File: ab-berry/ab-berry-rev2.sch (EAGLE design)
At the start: 66 parts, among them IC1 STM32F302RCT6, U1 LM1117MPX-3.3/NOPB or AP2114H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

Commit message: wip
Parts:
- removed STM32F072CBT6: STM32F072-LQFP48, stm32f0:STM32F072-LQFP48
- added R23, R24: 22, microbuilder:RESISTOR0603
- added X1: (no value), keves:TE-292304-1
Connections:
- new net N$18: R23.2, X1_CONN.2
- new net N$19: R24.2, X1_CONN.3
- new net SPI1_SCK: IC1.PB3, LCD2.CLK
- new net USB_DM: IC1.PA11, R23.1
- new net USB_DP: IC1.PA12, R24.1
- net 5.0V: now also X1_CONN.1
- net BTN_USR: now also IC1.PC13; no longer STM32F072CBT6.PC13/WKUP2/RTC_TAMP1/RTC_TS/RTC_OUT
- net CAN_RX: now also IC1.PB8; no longer STM32F072CBT6.PA11/USB_DM/CAN_RX
- net CAN_TX: now also IC1.PB9; no longer STM32F072CBT6.PA12/USB_DP/CAN_TX
- net DBG_RX: no longer STM32F072CBT6.PA10/USART1_RX/TIM1_CH3
- net DBG_TX: no longer STM32F072CBT6.PA9/USART1_TX/TIM1_CH2
- net GND: now also X1_CONN.4
- net LCD_CS1: now also IC1.PC11; no longer STM32F072CBT6.PB2
- net LCD_CS2: now also IC1.PC12; no longer STM32F072CBT6.PB1/ADC_IN9/TIM3_CH4
- net LCD_DC: now also IC1.PB7; no longer STM32F072CBT6.PA4/ADC_IN4/DAC_OUT1
- net LCD_RST: now also IC1.PB6; no longer STM32F072CBT6.PA3/ADC_IN3/COMP2_INP/USART2_RX
- net N$6: no longer STM32F072CBT6.PB0/ADC_IN8/TIM3_CH3
- net N$8: now also IC1.PF0_OSCIN; no longer STM32F072CBT6.PF0/OSC_IN
- net N$9: now also IC1.PF1_OSCOUT; no longer STM32F072CBT6.PF1/OSC_OUT
- net ROT1_A: no longer STM32F072CBT6.PB14/SPI2_MISO/I2C2_SDA
- net ROT1_B: no longer STM32F072CBT6.PB15/WKUP7/RTC_REFIN/SPI2_MOSI
- net ROT1_SW: no longer STM32F072CBT6.PB12
- net ROT2_A: no longer STM32F072CBT6.PB4/SPI1_MISO/TIM3_CH1
- net ROT2_B: no longer STM32F072CBT6.PB5/WKUP6/SPI1_MOSI/TIM3_CH2
- net ROT2_SW: no longer STM32F072CBT6.PB3/SPI1_SCK/TIM2_CH2
- net ROT3_A: no longer STM32F072CBT6.PB7/USART1_RX/I2C1_SDA
- net ROT3_B: no longer STM32F072CBT6.PB8/I2C1_SCL/TIM16_CH1/CAN_RX
- net ROT3_SW: no longer STM32F072CBT6.PB6USART1_TX/I2C1_SCL
- net ROT4_A: no longer STM32F072CBT6.PB13/SPI2_SCK/I2C2_SCL
- net ROT4_B: no longer STM32F072CBT6.PB11/I2C2_SDA/TIM2_C4/USART3_RX
- net ROT4_SW: no longer STM32F072CBT6.PB10/I2C2_SCL/TIM2_CH3/USART3_TX
- net SPI1_CLK: no longer LCD2.CLK, STM32F072CBT6.PA5/ADC_IN5/DAC_OUT2/SPI1_SCK
- net SPI1_MOSI: now also IC1.PB5; no longer STM32F072CBT6.PA7/ADC_IN7/SPI1_MOSI/TIM3_CH2
- net SWCLK: no longer STM32F072CBT6.PA14/USART2_TX/SWCLK
- net SWDIO: no longer STM32F072CBT6.PA13/SWDIO
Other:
- note added: "TODO: - Verify USB resistors / DP/DM - Verify Boot0 and are there any other mandatory connections"
- moved on the sheet: C12, C13, U$36

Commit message: wip
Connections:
- net DBG_RX: now also IC1.PB11
- net DBG_TX: now also IC1.PB10
- net N$6: now also IC1.PB12
- net ROT1_A: now also IC1.PA2
- net ROT1_B: now also IC1.PA1
- net ROT1_SW: now also IC1.PA0
- net ROT2_A: now also IC1.PC7
- net ROT2_B: now also IC1.PC9
- net ROT2_SW: now also IC1.PC8
- net ROT3_A: now also IC1.PA9
- net ROT3_B: now also IC1.PA10
- net ROT3_SW: now also IC1.PA8
- net ROT4_A: now also IC1.PC2
- net ROT4_B: now also IC1.PC1
- net ROT4_SW: now also IC1.PC0
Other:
- note added: "TODO: - Verify USB resistors / DP/DM - Verify Boot0 and are there any other mandatory connections - USB shield + ESD"
- note removed: "TODO: - Verify USB resistors / DP/DM - Verify Boot0 and are there any other mandatory connections"
- moved on the sheet: C1, C12, C13, C2, C22, C3, C4, C5, C6, IC1, LED2, R1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

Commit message: wip
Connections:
- removed net SPI1_CLK: LCD1.CLK
- net SPI1_SCK: now also LCD1.CLK
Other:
- note added: "TODO: - Verify USB resistors / DP/DM - Verify Boot0 and are there any other mandatory connections - USB shield + ESD - Serial Flash"
- note removed: "TODO: - Verify USB resistors / DP/DM - Verify Boot0 and are there any other mandatory connections - USB shield + ESD"
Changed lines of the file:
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@@
 - Verify USB resistors / DP/DM
 - Verify Boot0 and are there any other mandatory connections
-- USB shield + ESD</text>
+- USB shield + ESD
+- Serial Flash</text>
 </plain>
 <instances>
@@
 </segment>
 </net>
-<net name="SPI1_CLK" class="0">
-<segment>
-<pinref part="LCD1" gate="G$1" pin="CLK"/>
-<wire x1="111.76" y1="-20.32" x2="99.06" y2="-20.32" width="0.1524" layer="91"/>
-<label x="91.44" y="-20.32" size="1.778" layer="95"/>
-</segment>
-</net>
 <net name="LCD_CS2" class="0">
 <segment>
@@
 <label x="91.44" y="-55.88" size="1.778" layer="95"/>
 </segment>
-</net>
+<segment>
+<pinref part="LCD1" gate="G$1" pin="CLK"/>
+<wire x1="111.76" y1="-20.32" x2="99.06" y2="-20.32" width="0.1524" layer="91"/>
+<label x="91.44" y="-20.32" size="1.778" layer="95"/>
+</segment>
+</net>

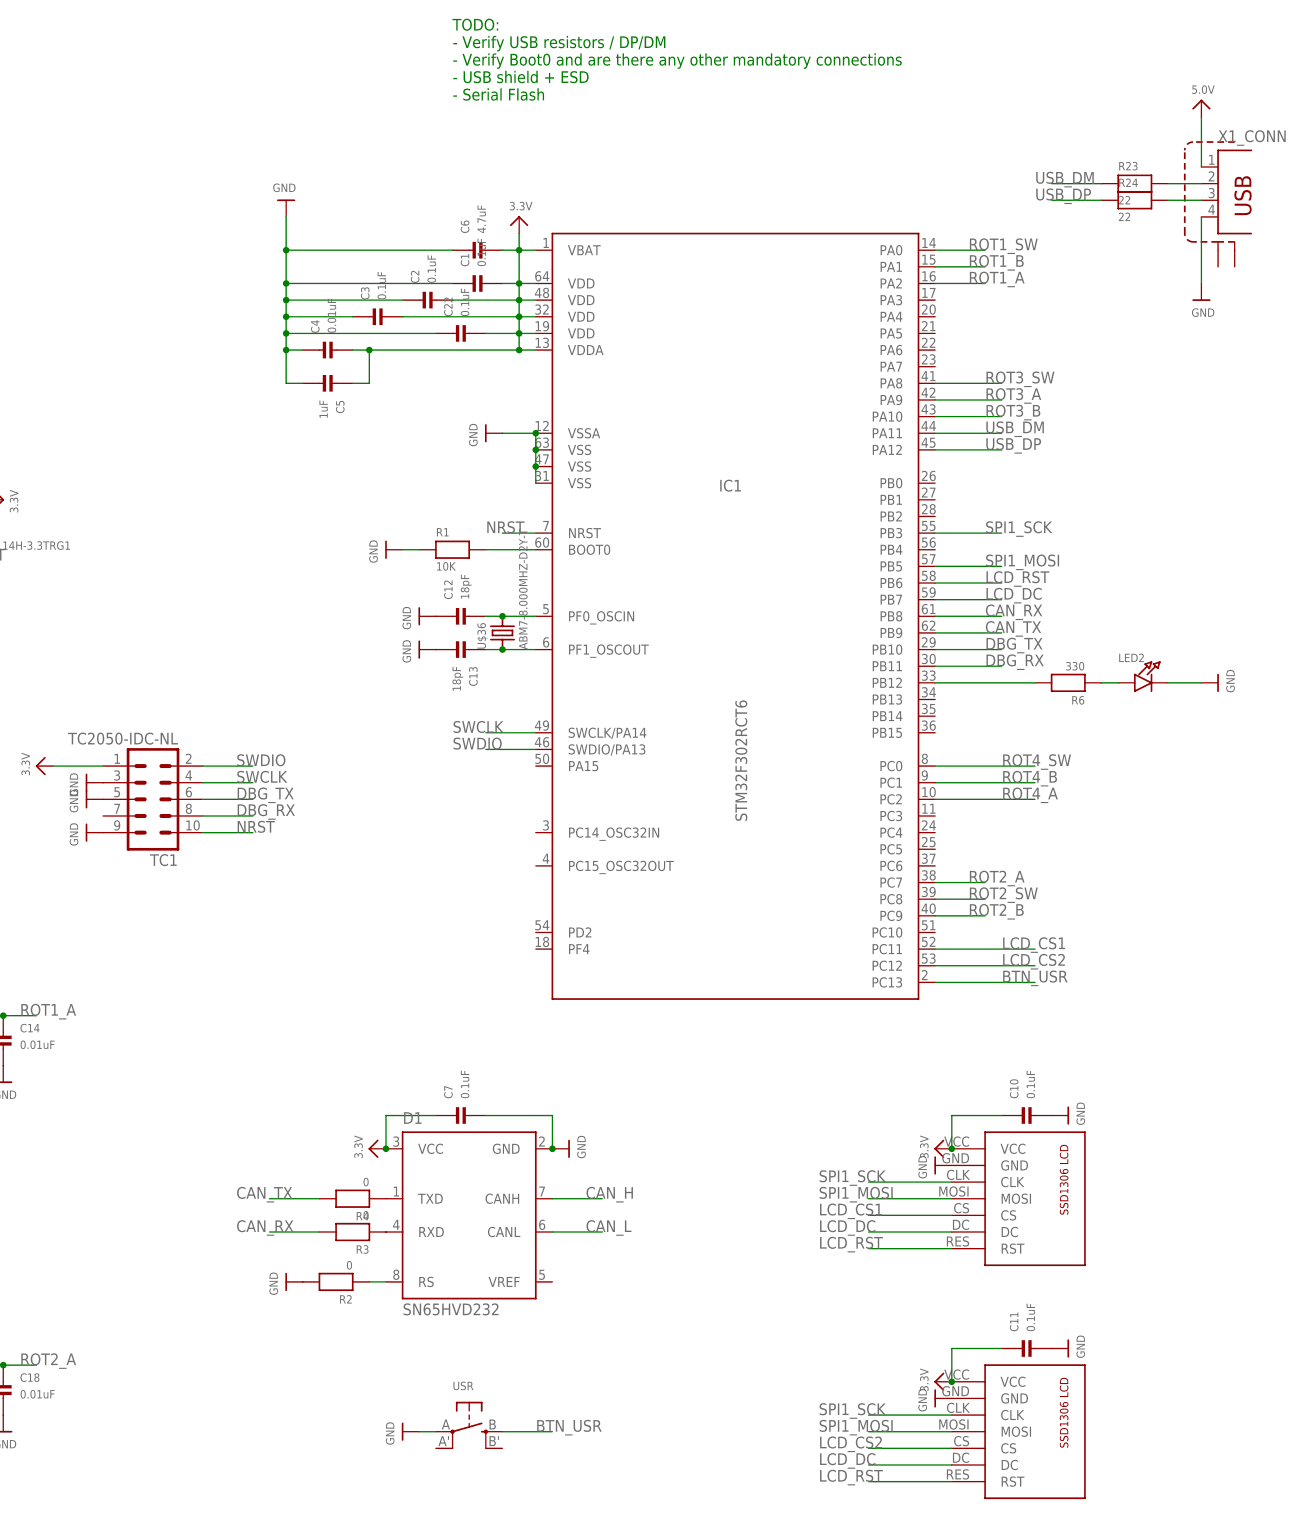
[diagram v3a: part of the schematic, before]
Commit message: switch ab-berry-rev2 to STM32F303CCT6
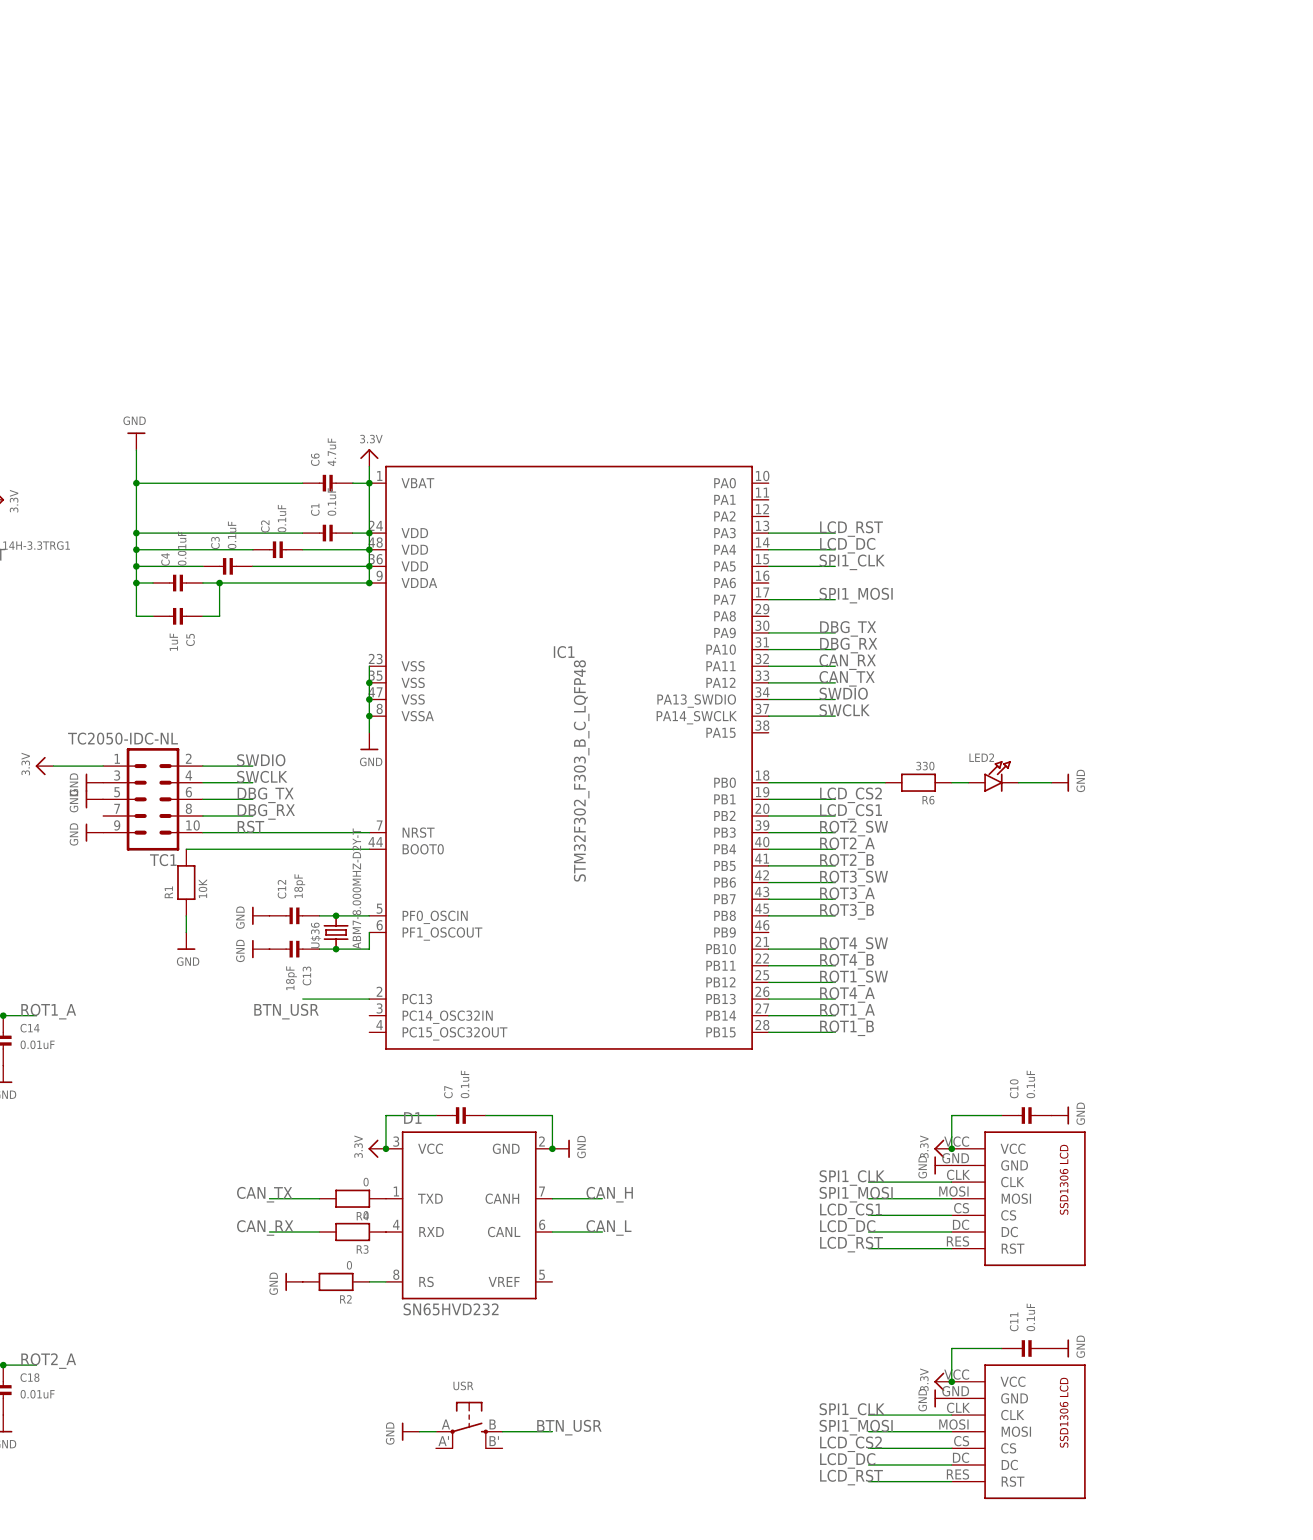
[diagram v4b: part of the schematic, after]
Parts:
- removed C22: 0.1uF, microbuilder:CAP_CERAMIC0603
- removed R23, R24: 22, microbuilder:RESISTOR0603
- removed X1: (no value), keves:TE-292304-1
- IC1: value STM32F302RCT6 -> STM32F302_F303_B_C_LQFP48; device keves:STM32F302_F303_B_C_LQFP64 -> keves:STM32F302_F303_B_C_LQFP48
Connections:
- net NRST renamed RST
- removed net N$18: R23.2, X1_CONN.2
- removed net N$19: R24.2, X1_CONN.3
- removed net SPI1_SCK: IC1.PB3, LCD1.CLK, LCD2.CLK
- removed net USB_DM: IC1.PA11, R23.1
- removed net USB_DP: IC1.PA12, R24.1
- new net SPI1_CLK: IC1.PA5, LCD1.CLK, LCD2.CLK
- net 3.3V: no longer C22.P$2, IC1.VDD@4
- net 5.0V: no longer X1_CONN.1
- net CAN_RX: now also IC1.PA11; no longer IC1.PB8
- net CAN_TX: now also IC1.PA12; no longer IC1.PB9
- net DBG_RX: now also IC1.PA10; no longer IC1.PB11
- net DBG_TX: now also IC1.PA9; no longer IC1.PB10
- net GND: no longer C22.P$1, X1_CONN.4
- net LCD_CS1: now also IC1.PB2; no longer IC1.PC11
- net LCD_CS2: now also IC1.PB1; no longer IC1.PC12
- net LCD_DC: now also IC1.PA4; no longer IC1.PB7
- net LCD_RST: now also IC1.PA3; no longer IC1.PB6
- net N$6: now also IC1.PB0; no longer IC1.PB12
- net ROT1_A: now also IC1.PB14; no longer IC1.PA2
- net ROT1_B: now also IC1.PB15; no longer IC1.PA1
- net ROT1_SW: now also IC1.PB12; no longer IC1.PA0
- net ROT2_A: now also IC1.PB4; no longer IC1.PC7
- net ROT2_B: now also IC1.PB5; no longer IC1.PC9
- net ROT2_SW: now also IC1.PB3; no longer IC1.PC8
- net ROT3_A: now also IC1.PB7; no longer IC1.PA9
- net ROT3_B: now also IC1.PB8; no longer IC1.PA10
- net ROT3_SW: now also IC1.PB6; no longer IC1.PA8
- net ROT4_A: now also IC1.PB13; no longer IC1.PC2
- net ROT4_B: now also IC1.PB11; no longer IC1.PC1
- net ROT4_SW: now also IC1.PB10; no longer IC1.PC0
- net SPI1_MOSI: now also IC1.PA7; no longer IC1.PB5
- net SWCLK: now also IC1.PA14_SWCLK; no longer IC1.SWCLK/PA14
- net SWDIO: now also IC1.PA13_SWDIO; no longer IC1.SWDIO/PA13
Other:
- note removed: "TODO: - Verify USB resistors / DP/DM - Verify Boot0 and are there any other mandatory connections - USB shield + ESD - Serial Flash"
- moved on the sheet: C1, C12, C13, C2, C3, C4, C5, C6, LED2, R1, R6, U$36
